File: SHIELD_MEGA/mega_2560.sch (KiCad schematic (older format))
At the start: 1 part

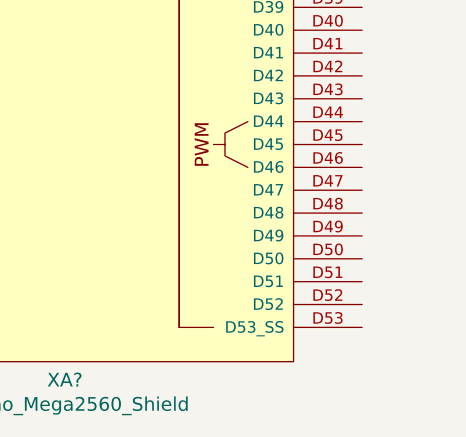
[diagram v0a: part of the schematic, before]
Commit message: Addings pins of receiver in mega
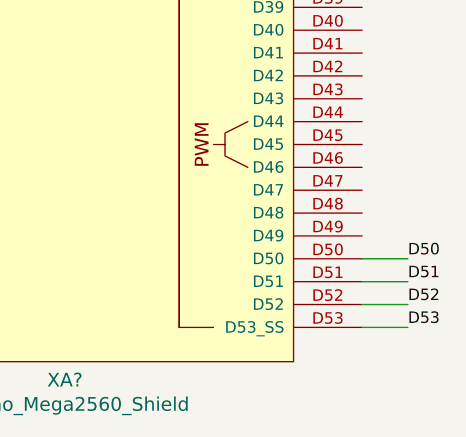
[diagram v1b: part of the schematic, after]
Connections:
- net D50: now reaches XA?.D50
- net D51: now reaches XA?.D51
- net D52: now reaches XA?.D52
- net D53: now reaches XA?.D53 (D53_SS)
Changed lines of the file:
@@
 Wire Wire Line
 	4150 2650 4550 2650
+Text Label 7350 5850 0    50   ~ 0
+D53
+Wire Wire Line
+	7350 5850 7150 5850
+Wire Wire Line
+	7150 5750 7350 5750
+Text Label 7350 5750 0    50   ~ 0
+D52
+Wire Wire Line
+	7350 5650 7150 5650
+Text Label 7350 5650 0    50   ~ 0
+D51
+Wire Wire Line
+	7350 5550 7150 5550
+Text Label 7350 5550 0    50   ~ 0
+D50
 $EndSCHEMATC

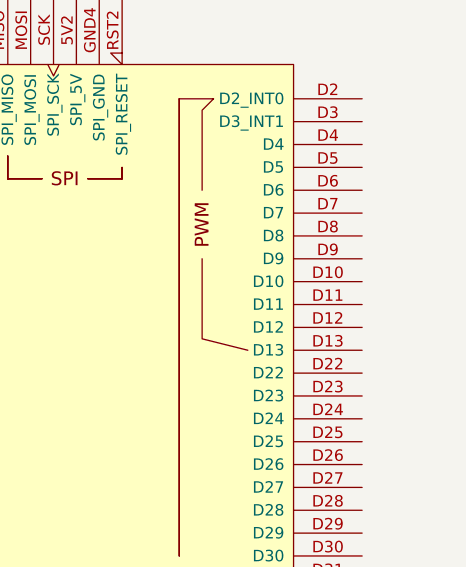
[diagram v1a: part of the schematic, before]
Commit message: Addings pins of receiver in mega FINISH
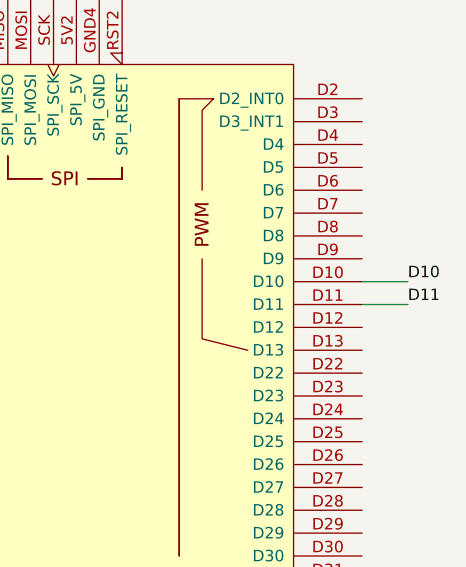
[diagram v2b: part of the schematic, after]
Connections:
- net D10: now reaches XA?.D10
- net D11: now reaches XA?.D11
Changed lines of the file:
@@
 Text Label 7350 5550 0    50   ~ 0
 D50
+Text Label 7350 2350 0    50   ~ 0
+D10
+Wire Wire Line
+	7350 2350 7150 2350
+Wire Wire Line
+	7150 2450 7350 2450
+Text Label 7350 2450 0    50   ~ 0
+D11
 $EndSCHEMATC

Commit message: Updating
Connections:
- net A0: now reaches XA?.A0
- net A1: now reaches XA?.A1
- net A10: now reaches XA?.A10
- net A11: now reaches XA?.A11
- net A12: now reaches XA?.A12
- net A13: now reaches XA?.A13
- net A14: now reaches XA?.A14
- net A15: now reaches XA?.A15
- net A2: now reaches XA?.A2
- net A3: now reaches XA?.A3
- net A4: now reaches XA?.A4
- net A5: now reaches XA?.A5
- net A6: now reaches XA?.A6
- net A7: now reaches XA?.A7
- net A8: now reaches XA?.A8
- net A9: now reaches XA?.A9
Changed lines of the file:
@@
 $Descr A4 11693 8268
 encoding utf-8
-Sheet 2 6
+Sheet 2 7
 Title ""
 Date ""
@@
 Text Label 7350 2450 0    50   ~ 0
 D11
+$Sheet
+S 2900 2750 650  1700
+U 61A24149
+F0 "ANALOG_PINS" 50
+F1 "ANALOG_BUS.sch" 50
+$EndSheet
+Text HLabel 3550 2850 0    50   Input ~ 0
+A0
+Text HLabel 3550 2950 0    50   Input ~ 0
+A1
+Text HLabel 3550 3050 0    50   Input ~ 0
+A2
+Text HLabel 3550 3150 0    50   Input ~ 0
+A3
+Text HLabel 3550 3250 0    50   Input ~ 0
+A4
+Text HLabel 3550 3350 0    50   Input ~ 0
+A5
+Text HLabel 3550 3450 0    50   Input ~ 0
+A6
+Text HLabel 3550 3550 0    50   Input ~ 0
+A7
+Text HLabel 3550 3650 0    50   Input ~ 0
+A8
+Text HLabel 3550 3750 0    50   Input ~ 0
+A9
+Text HLabel 3550 3850 0    50   Input ~ 0
+A10
+Text HLabel 3550 3950 0    50   Input ~ 0
+A11
+Text HLabel 3550 4050 0    50   Input ~ 0
+A12
+Text HLabel 3550 4150 0    50   Input ~ 0
+A13
+Text HLabel 3550 4250 0    50   Input ~ 0
+A14
+Text HLabel 3550 4350 0    50   Input ~ 0
+A15
+Wire Wire Line
+	3550 2850 4550 2850
+Wire Wire Line
+	4550 2950 3550 2950
+Wire Wire Line
+	3550 3050 4550 3050
+Wire Wire Line
+	4550 3150 3550 3150
+Wire Wire Line
+	3550 3250 4550 3250
+Wire Wire Line
+	4550 3350 3550 3350
+Wire Wire Line
+	3550 3450 4550 3450
+Wire Wire Line
+	4550 3550 3550 3550
+Wire Wire Line
+	3550 3650 4550 3650
+Wire Wire Line
+	4550 3750 3550 3750
+Wire Wire Line
+	3550 3850 4550 3850
+Wire Wire Line
+	4550 3950 3550 3950
+Wire Wire Line
+	3550 4050 4550 4050
+Wire Wire Line
+	4550 4150 3550 4150
+Wire Wire Line
+	3550 4250 4550 4250
+Wire Wire Line
+	4550 4350 3550 4350
 $EndSCHEMATC

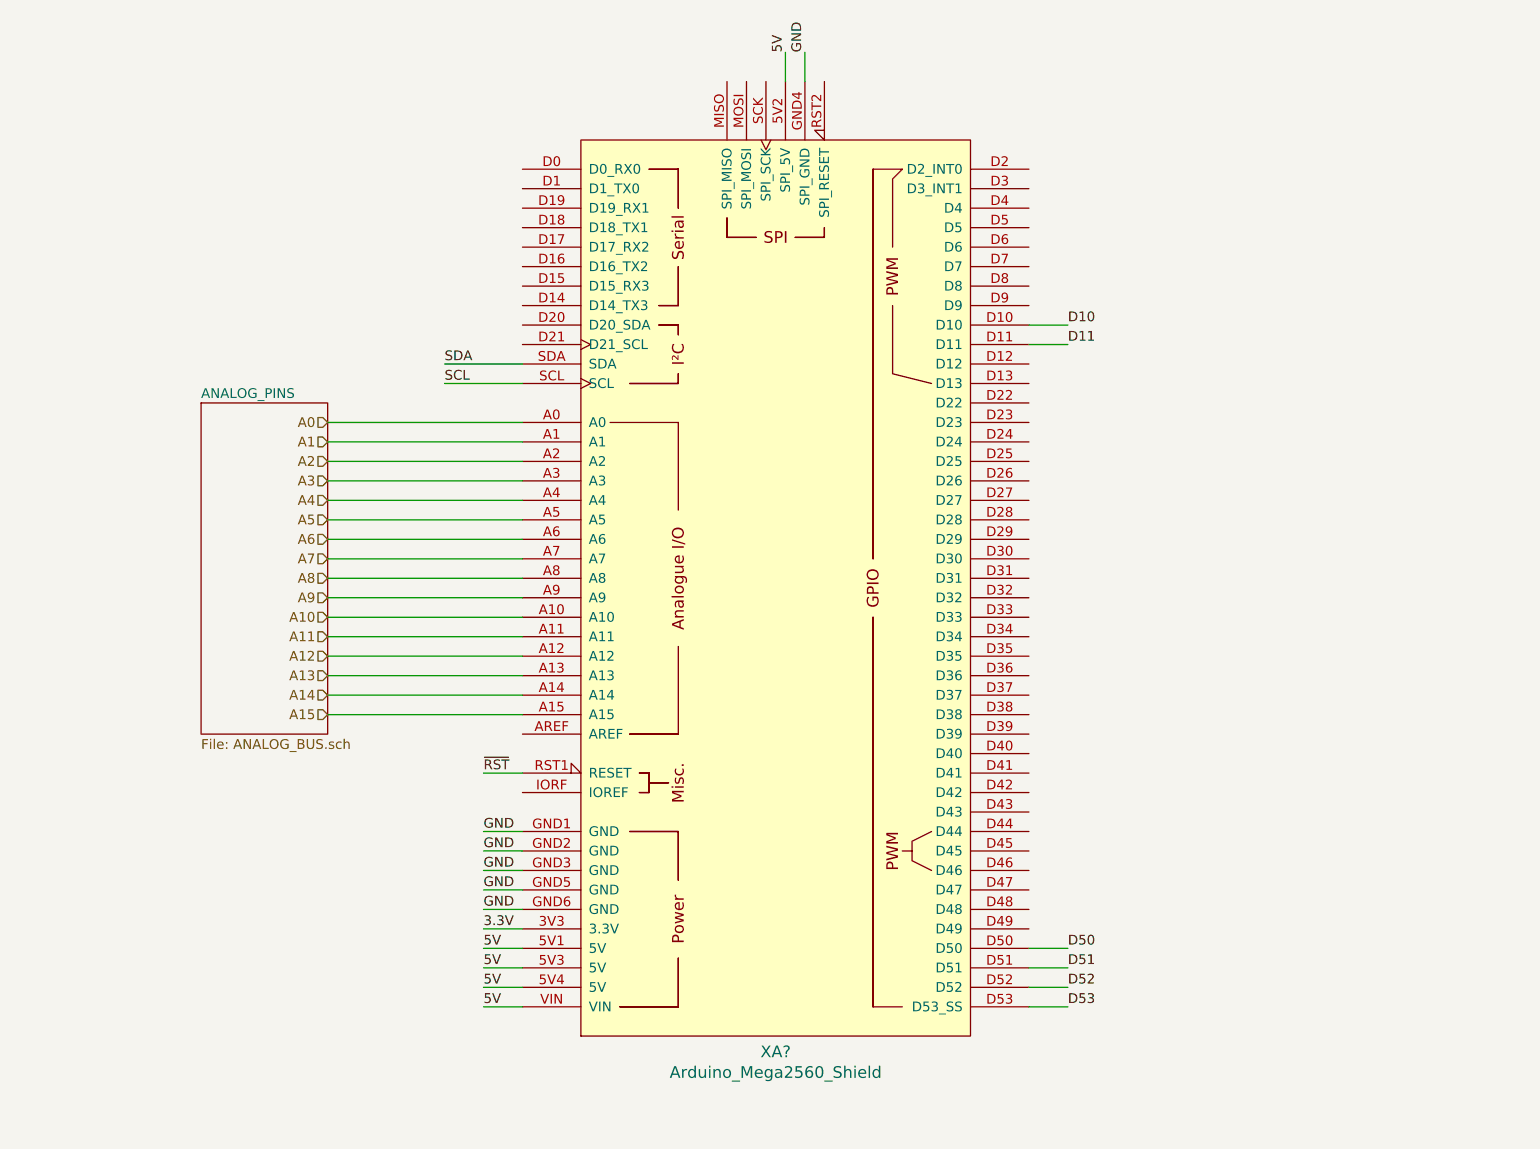
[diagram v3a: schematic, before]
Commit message: fixing label symbols type
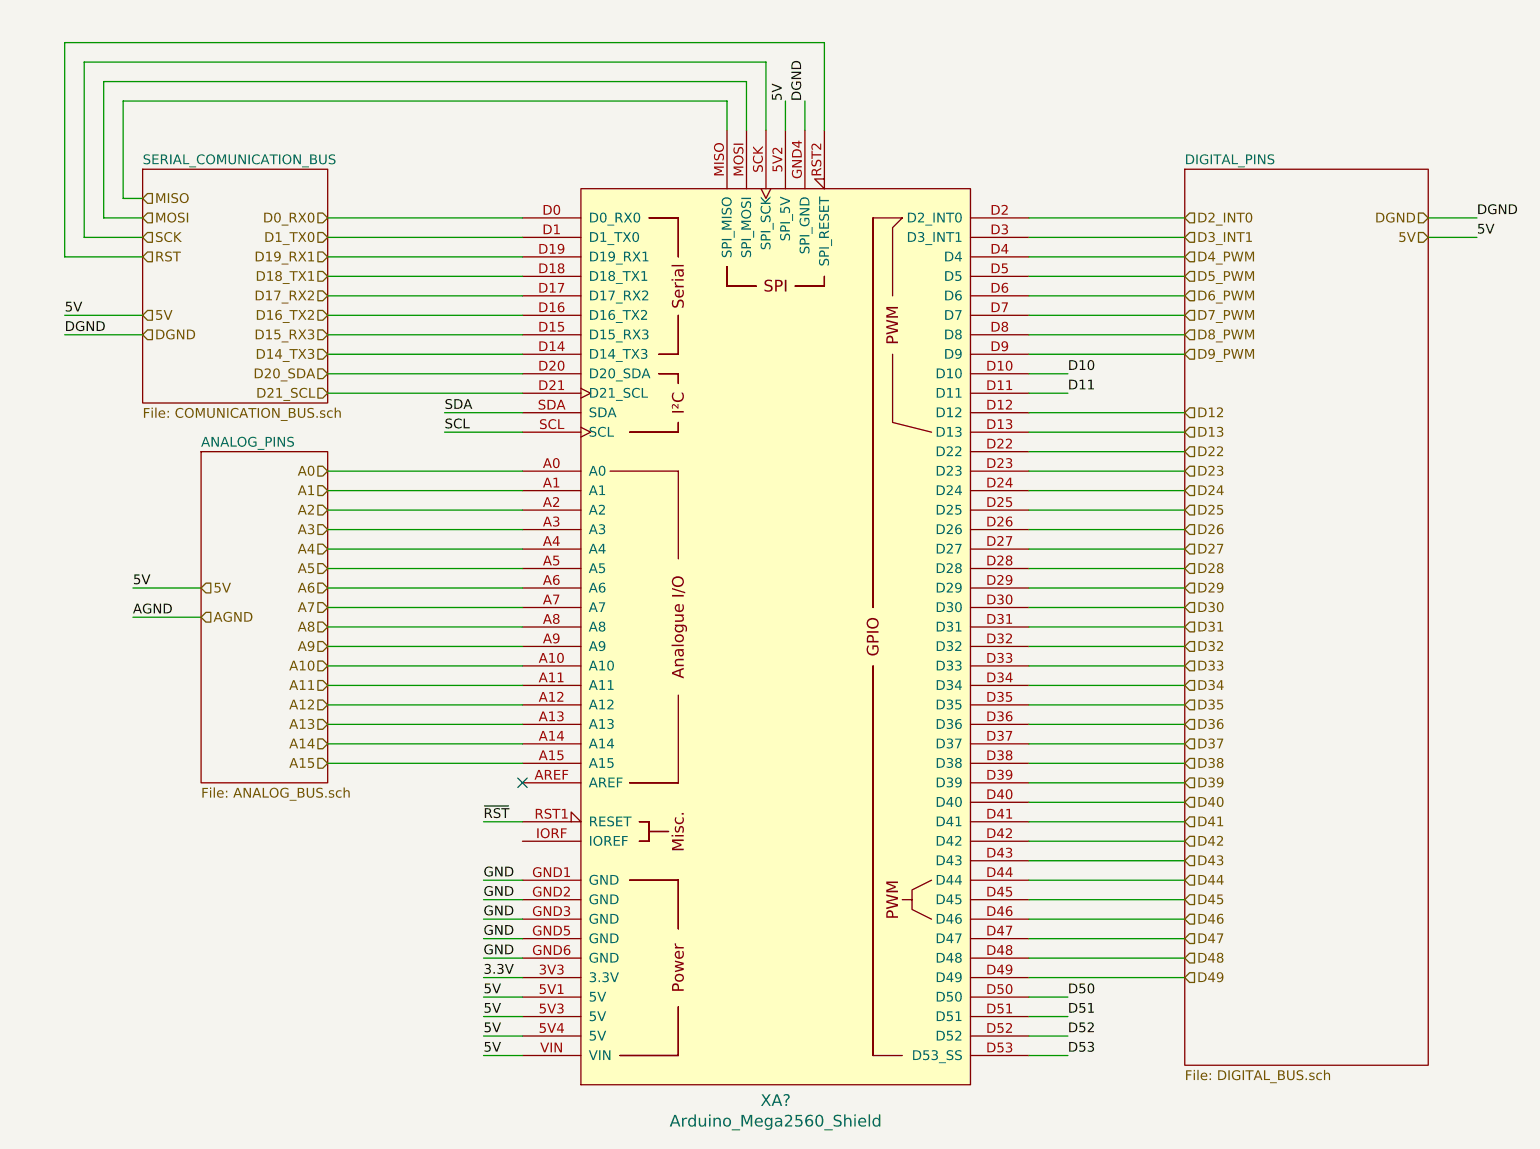
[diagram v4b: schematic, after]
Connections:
- net GND: no longer XA?.GND4 (SPI_GND)
- net D0_RX0: now reaches XA?.D0 (D0_RX0)
- net D1_TX0: now reaches XA?.D1 (D1_TX0)
- net D12: now reaches XA?.D12
- net D13: now reaches XA?.D13
- net D14_TX3: now reaches XA?.D14 (D14_TX3)
- net D15_RX3: now reaches XA?.D15 (D15_RX3)
- net D16_TX2: now reaches XA?.D16 (D16_TX2)
- net D17_RX2: now reaches XA?.D17 (D17_RX2)
- net D18_TX1: now reaches XA?.D18 (D18_TX1)
- net D19_RX1: now reaches XA?.D19 (D19_RX1)
- net D2_INT0: now reaches XA?.D2 (D2_INT0)
- net D20_SDA: now reaches XA?.D20 (D20_SDA)
- net D21_SCL: now reaches XA?.D21 (D21_SCL)
- net D22: now reaches XA?.D22
- net D23: now reaches XA?.D23
- net D24: now reaches XA?.D24
- net D25: now reaches XA?.D25
- net D26: now reaches XA?.D26
- net D27: now reaches XA?.D27
- net D28: now reaches XA?.D28
- net D29: now reaches XA?.D29
- net D3_INT1: now reaches XA?.D3 (D3_INT1)
- net D30: now reaches XA?.D30
- net D31: now reaches XA?.D31
- net D32: now reaches XA?.D32
- net D33: now reaches XA?.D33
- net D34: now reaches XA?.D34
- net D35: now reaches XA?.D35
- net D36: now reaches XA?.D36
- net D37: now reaches XA?.D37
- net D38: now reaches XA?.D38
- net D39: now reaches XA?.D39
- net D4_PWM: now reaches XA?.D4
- net D40: now reaches XA?.D40
- net D41: now reaches XA?.D41
- net D42: now reaches XA?.D42
- net D43: now reaches XA?.D43
- net D44: now reaches XA?.D44
- net D45: now reaches XA?.D45
- net D46: now reaches XA?.D46
- net D47: now reaches XA?.D47
- net D48: now reaches XA?.D48
- net D49: now reaches XA?.D49
- net D5_PWM: now reaches XA?.D5
- net D6_PWM: now reaches XA?.D6
- net D7_PWM: now reaches XA?.D7
- net D8_PWM: now reaches XA?.D8
- net D9_PWM: now reaches XA?.D9
- net MISO: now reaches XA?.MISO (SPI_MISO)
- net MOSI: now reaches XA?.MOSI (SPI_MOSI)
- net RST: now reaches XA?.RST2 (SPI_RESET)
- net SCK: now reaches XA?.SCK (SPI_SCK)
- new net DGND: XA?.GND4 (SPI_GND)
- no-connect marks 0 -> 1
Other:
- moved on the sheet: XA?

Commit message: Upddates in projct sheet info
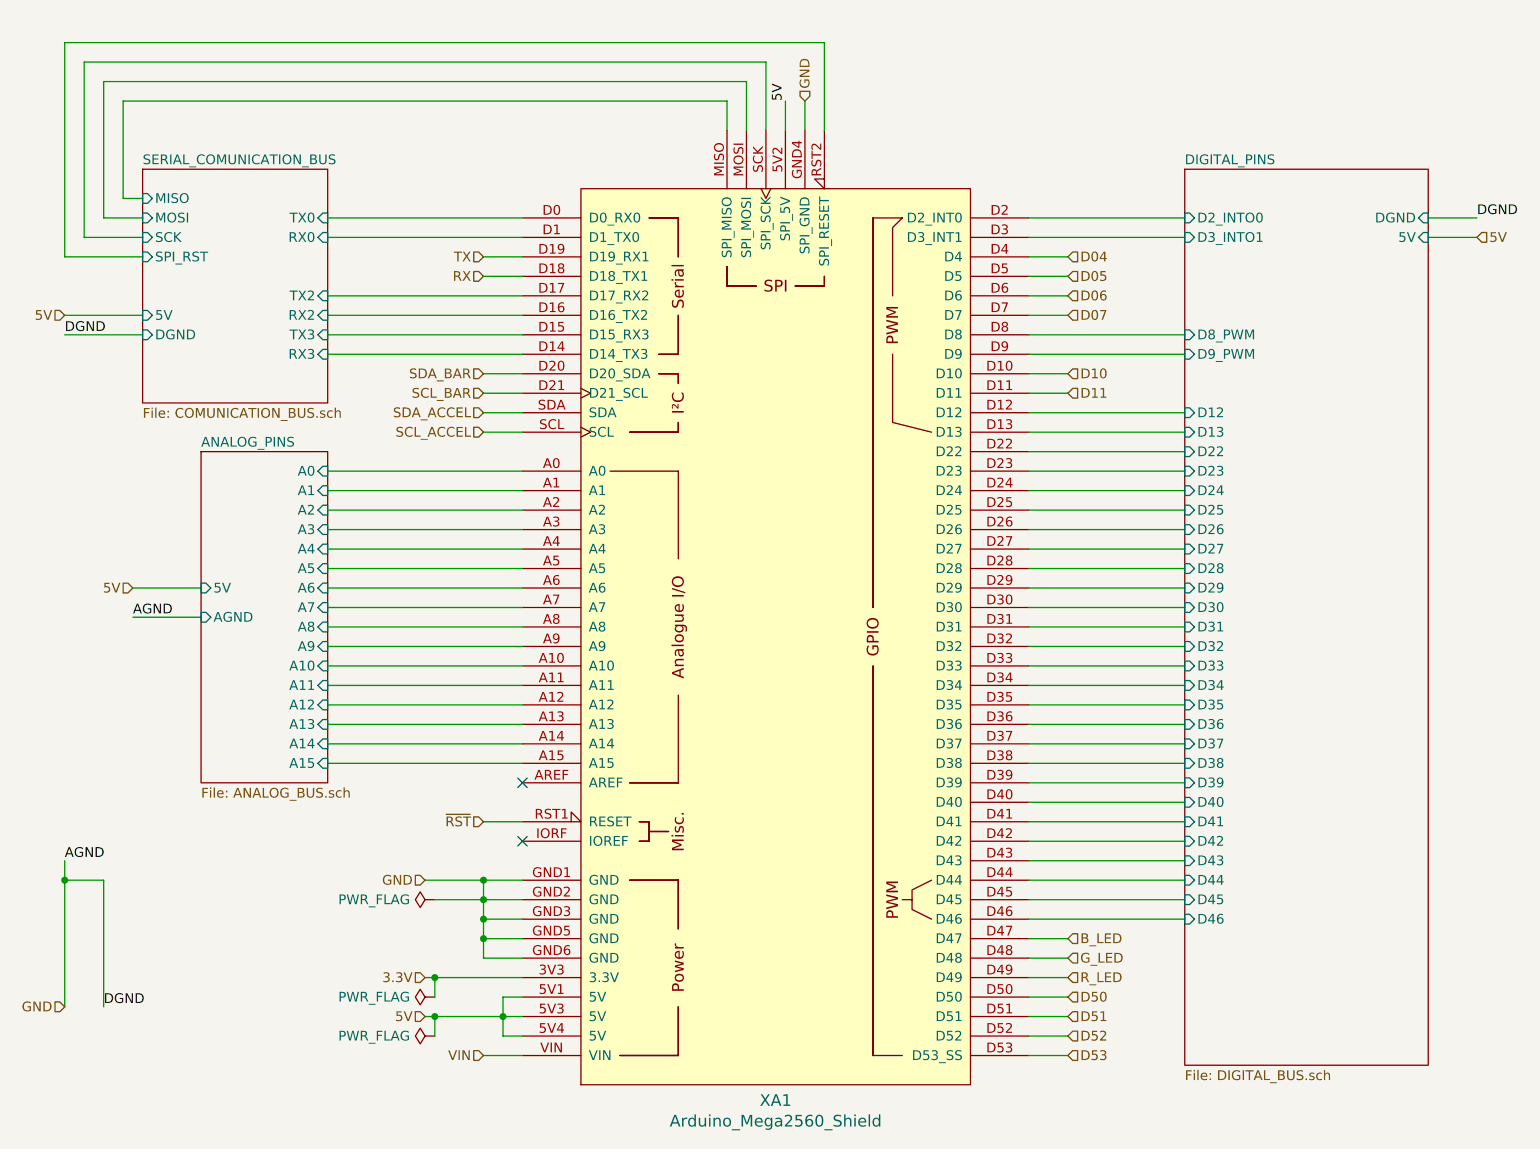
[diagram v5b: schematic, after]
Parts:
- XA1: renamed from XA?; footprint (none) -> Arduino:Arduino_Mega2560_Shield
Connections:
- net DGND is gone; now on net GND: XA1.GND4 (SPI_GND)
- net 5V: no longer XA1.VIN
- net A0 renamed ANALOG_PINS/A0
- net A1 renamed ANALOG_PINS/A1
- net A10 renamed ANALOG_PINS/A10
- net A11 renamed ANALOG_PINS/A11
- net A12 renamed ANALOG_PINS/A12
- net A13 renamed ANALOG_PINS/A13
- net A14 renamed ANALOG_PINS/A14
- net A15 renamed ANALOG_PINS/A15
- net A2 renamed ANALOG_PINS/A2
- net A3 renamed ANALOG_PINS/A3
- net A4 renamed ANALOG_PINS/A4
- net A5 renamed ANALOG_PINS/A5
- net A6 renamed ANALOG_PINS/A6
- net A7 renamed ANALOG_PINS/A7
- net A8 renamed ANALOG_PINS/A8
- net A9 renamed ANALOG_PINS/A9
- net D0_RX0 renamed SERIAL_COMUNICATION_BUS/TX0
- net D12 renamed DIGITAL_PINS/D12
- net D13 renamed DIGITAL_PINS/D13
- net D14_TX3 renamed SERIAL_COMUNICATION_BUS/RX3
- net D15_RX3 renamed SERIAL_COMUNICATION_BUS/TX3
- net D16_TX2 renamed SERIAL_COMUNICATION_BUS/RX2
- net D17_RX2 renamed SERIAL_COMUNICATION_BUS/TX2
- net D18_TX1 renamed RX
- net D19_RX1 renamed TX
- net D1_TX0 renamed SERIAL_COMUNICATION_BUS/RX0
- net D20_SDA renamed SDA_BAR
- net D21_SCL renamed SCL_BAR
- net D22 renamed DIGITAL_PINS/D22
- net D23 renamed DIGITAL_PINS/D23
- net D24 renamed DIGITAL_PINS/D24
- net D25 renamed DIGITAL_PINS/D25
- net D26 renamed DIGITAL_PINS/D26
- net D27 renamed DIGITAL_PINS/D27
- net D28 renamed DIGITAL_PINS/D28
- net D29 renamed DIGITAL_PINS/D29
- net D2_INT0 renamed DIGITAL_PINS/D2_INTO0
- net D30 renamed DIGITAL_PINS/D30
- net D31 renamed DIGITAL_PINS/D31
- net D32 renamed DIGITAL_PINS/D32
- net D33 renamed DIGITAL_PINS/D33
- net D34 renamed DIGITAL_PINS/D34
- net D35 renamed DIGITAL_PINS/D35
- net D36 renamed DIGITAL_PINS/D36
- net D37 renamed DIGITAL_PINS/D37
- net D38 renamed DIGITAL_PINS/D38
- net D39 renamed DIGITAL_PINS/D39
- net D3_INT1 renamed DIGITAL_PINS/D3_INTO1
- net D40 renamed DIGITAL_PINS/D40
- net D41 renamed DIGITAL_PINS/D41
- net D42 renamed DIGITAL_PINS/D42
- net D43 renamed DIGITAL_PINS/D43
- net D44 renamed DIGITAL_PINS/D44
- net D45 renamed DIGITAL_PINS/D45
- net D46 renamed DIGITAL_PINS/D46
- net D47 renamed B_LED
- net D48 renamed G_LED
- net D49 renamed R_LED
- net D4_PWM renamed D04
- net D5_PWM renamed D05
- net D6_PWM renamed D06
- net D7_PWM renamed D07
- net D8_PWM renamed DIGITAL_PINS/D8_PWM
- net D9_PWM renamed DIGITAL_PINS/D9_PWM
- net MISO renamed SERIAL_COMUNICATION_BUS/MISO
- net MOSI renamed SERIAL_COMUNICATION_BUS/MOSI
- net RST renamed SERIAL_COMUNICATION_BUS/SPI_RST
- net SCK renamed SERIAL_COMUNICATION_BUS/SCK
- net SCL renamed SCL_ACCEL
- net SDA renamed SDA_ACCEL
- new net VIN: XA1.VIN
- no-connect marks 1 -> 2
